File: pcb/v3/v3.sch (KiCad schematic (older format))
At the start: 44 parts, among them J1 RJ10, J10 USB_A, J2 ICSP, J3 RJ10, J4 RJ10, J5 RJ10, J6 RJ10, J7 RJ10, J8 BOOST, J9 USB_B, Q2 2N3904, Q3 BS170, SW1 CTL1, SW2 CTL2, SW3 CTL3, U1 ATmega328P-PU, U2 PCF8574, U3 RC1602A, Y1 16MHz

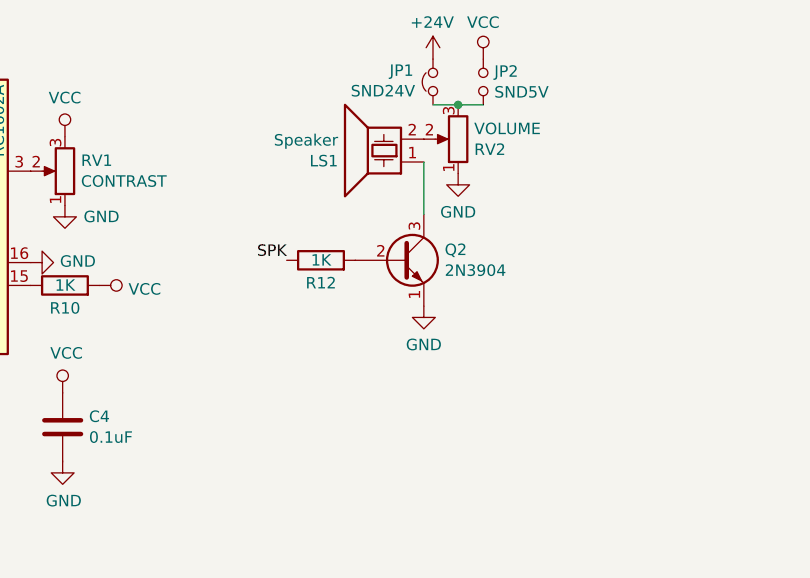
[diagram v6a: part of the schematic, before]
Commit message: add a capacitor to fix sound
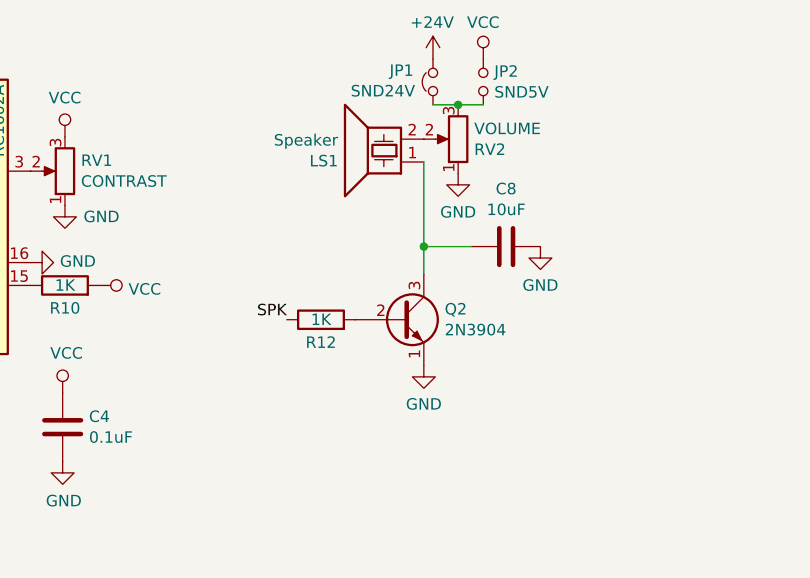
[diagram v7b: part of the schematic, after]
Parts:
- added C8: 10uF, Capacitor_SMD:C_1206_3216Metric_Pad1.42x1.75mm_HandSolder, symbol Device:C
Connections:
- wire segments 54 -> 56
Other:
- moved on the sheet: Q2, R12
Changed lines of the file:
@@
 EESchema Schematic File Version 4
-LIBS:v3-cache
 EELAYER 29 0
 EELAYER END
@@
 L Transistor_BJT:2N3904 Q2
 U 1 1 5C5AA536
-P 7380 3940
-F 0 "Q2" H 7571 3986 50  0000 L CNN
-F 1 "2N3904" H 7571 3895 50  0000 L CNN
-F 2 "Package_TO_SOT_THT:TO-92_Inline_Wide" H 7580 3865 50  0001 L CIN
-F 3 "https://www.fairchildsemi.com/datasheets/2N/2N3904.pdf" H 7380 3940 50  0001 L CNN
-	1    7380 3940
+P 7380 4200
+F 0 "Q2" H 7571 4246 50  0000 L CNN
+F 1 "2N3904" H 7571 4155 50  0000 L CNN
+F 2 "Package_TO_SOT_THT:TO-92_Inline_Wide" H 7580 4125 50  0001 L CIN
+F 3 "https://www.fairchildsemi.com/datasheets/2N/2N3904.pdf" H 7380 4200 50  0001 L CNN
+	1    7380 4200
 	1    0    0    -1
 $EndComp
@@
 L power:GND #PWR0145
 U 1 1 5C5ABB73
-P 7480 4140
-F 0 "#PWR0145" H 7480 3890 50  0001 C CNN
-F 1 "GND" H 7480 3970 50  0000 C CNN
-F 2 "" H 7480 4140 50  0001 C CNN
-F 3 "" H 7480 4140 50  0001 C CNN
-	1    7480 4140
+P 7480 4400
+F 0 "#PWR0145" H 7480 4150 50  0001 C CNN
+F 1 "GND" H 7480 4230 50  0000 C CNN
+F 2 "" H 7480 4400 50  0001 C CNN
+F 3 "" H 7480 4400 50  0001 C CNN
+	1    7480 4400
 	1    0    0    -1
 $EndComp
@@
 L Device:R R12
 U 1 1 5C5ADC70
-P 7030 3940
-F 0 "R12" V 6930 3940 50  0000 C CNN
-F 1 "1K" V 7030 3940 50  0000 C CNN
-F 2 "Resistor_SMD:R_1206_3216Metric_Pad1.42x1.75mm_HandSolder" V 6960 3940 50  0001 C CNN
-F 3 "~" H 7030 3940 50  0001 C CNN
-	1    7030 3940
+P 7030 4200
+F 0 "R12" V 6930 4200 50  0000 C CNN
+F 1 "1K" V 7030 4200 50  0000 C CNN
+F 2 "Resistor_SMD:R_1206_3216Metric_Pad1.42x1.75mm_HandSolder" V 6960 4200 50  0001 C CNN
+F 3 "~" H 7030 4200 50  0001 C CNN
+	1    7030 4200
 	0    -1   -1   0
 $EndComp
-Text Label 6880 3940 2    50   ~ 0
+Text Label 6880 4200 2    50   ~ 0
 SPK
 Text Label 3250 3850 0    50   ~ 0
@@
 	1    0    0    -1
 $EndComp
-Wire Wire Line
-	7480 3510 7480 3740
 NoConn ~ 3250 1650
+$Comp
+L Device:C C8
+U 1 1 5D7523CE
+P 7840 3880
+F 0 "C8" V 7588 3880 50  0000 C CNN
+F 1 "10uF" V 7679 3880 50  0000 C CNN
+F 2 "Capacitor_SMD:C_1206_3216Metric_Pad1.42x1.75mm_HandSolder" H 7878 3730 50  0001 C CNN
+F 3 "~" H 7840 3880 50  0001 C CNN
+	1    7840 3880
+	0    1    1    0
+$EndComp
+Wire Wire Line
+	7480 3510 7480 3880
+Wire Wire Line
+	7690 3880 7480 3880
+Connection ~ 7480 3880
+Wire Wire Line
+	7480 3880 7480 4000
+$Comp
+L power:GND #PWR03
+U 1 1 5D755CC5
+P 7990 3880
+F 0 "#PWR03" H 7990 3630 50  0001 C CNN
+F 1 "GND" H 7990 3710 50  0000 C CNN
+F 2 "" H 7990 3880 50  0001 C CNN
+F 3 "" H 7990 3880 50  0001 C CNN
+	1    7990 3880
+	1    0    0    -1
+$EndComp
 $EndSCHEMATC
